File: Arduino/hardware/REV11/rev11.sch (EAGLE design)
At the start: 24 parts, among them IC2 ATMEGA168-AU, Q1 32768Hz

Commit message: updated rev11 as per mark & damons spec's
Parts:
- renumbered FTDI+I2C to I2C_EXT
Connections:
- removed net N$5: I2C_EXT.9, R4.2
- new net N$4: I2C_EXT.11, R4.2
- net GND: now also I2C_EXT.6; no longer I2C_EXT.1, I2C_EXT.3
- net N$1: now also I2C_EXT.5; no longer I2C_EXT.11
- net N$3: now also I2C_EXT.12; no longer I2C_EXT.7
- net RFM_IRQ: now also I2C_EXT.7
- net SCL: now also I2C_EXT.9; no longer I2C_EXT.2
- net SDA: now also I2C_EXT.10; no longer I2C_EXT.4
- net SPI_MISO: now also I2C_EXT.1
- net SPI_MOSI: now also I2C_EXT.4
- net SPI_NSS: now also I2C_EXT.8
- net SPI_SCK: now also I2C_EXT.3
- net VCC: now also I2C_EXT.2; no longer I2C_EXT.14
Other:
- moved on the sheet: C11, R4, R5

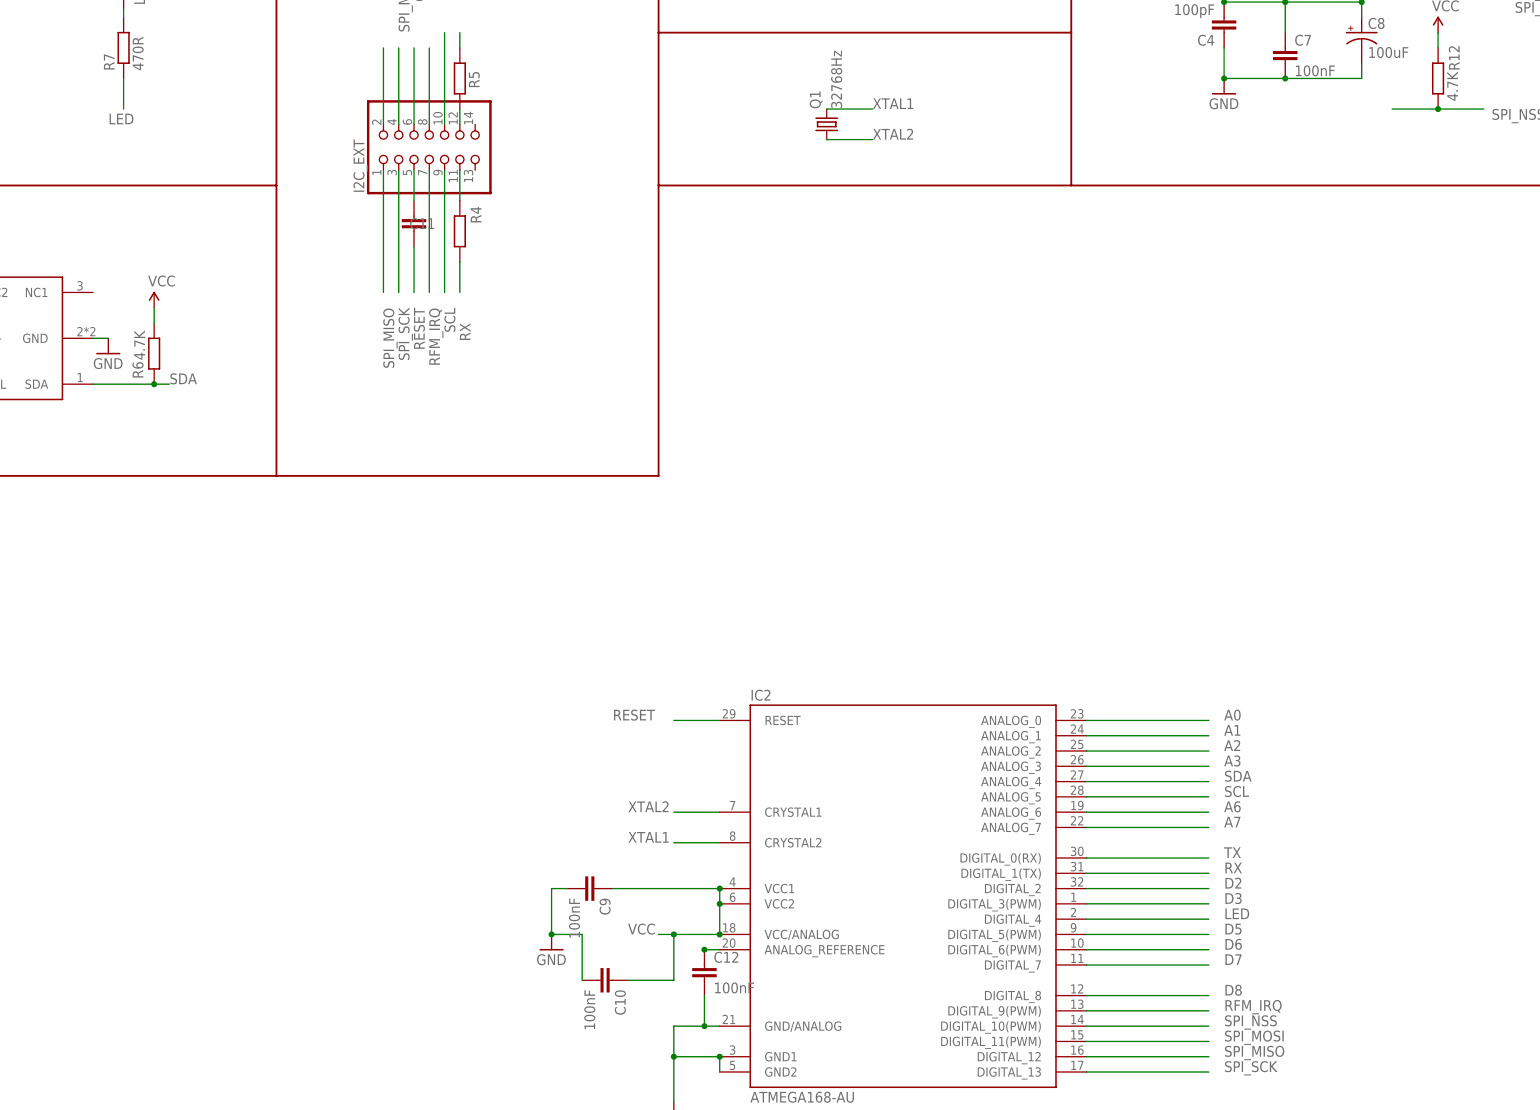
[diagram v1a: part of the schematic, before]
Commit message: updated rev11 as per mark and damon spec 2
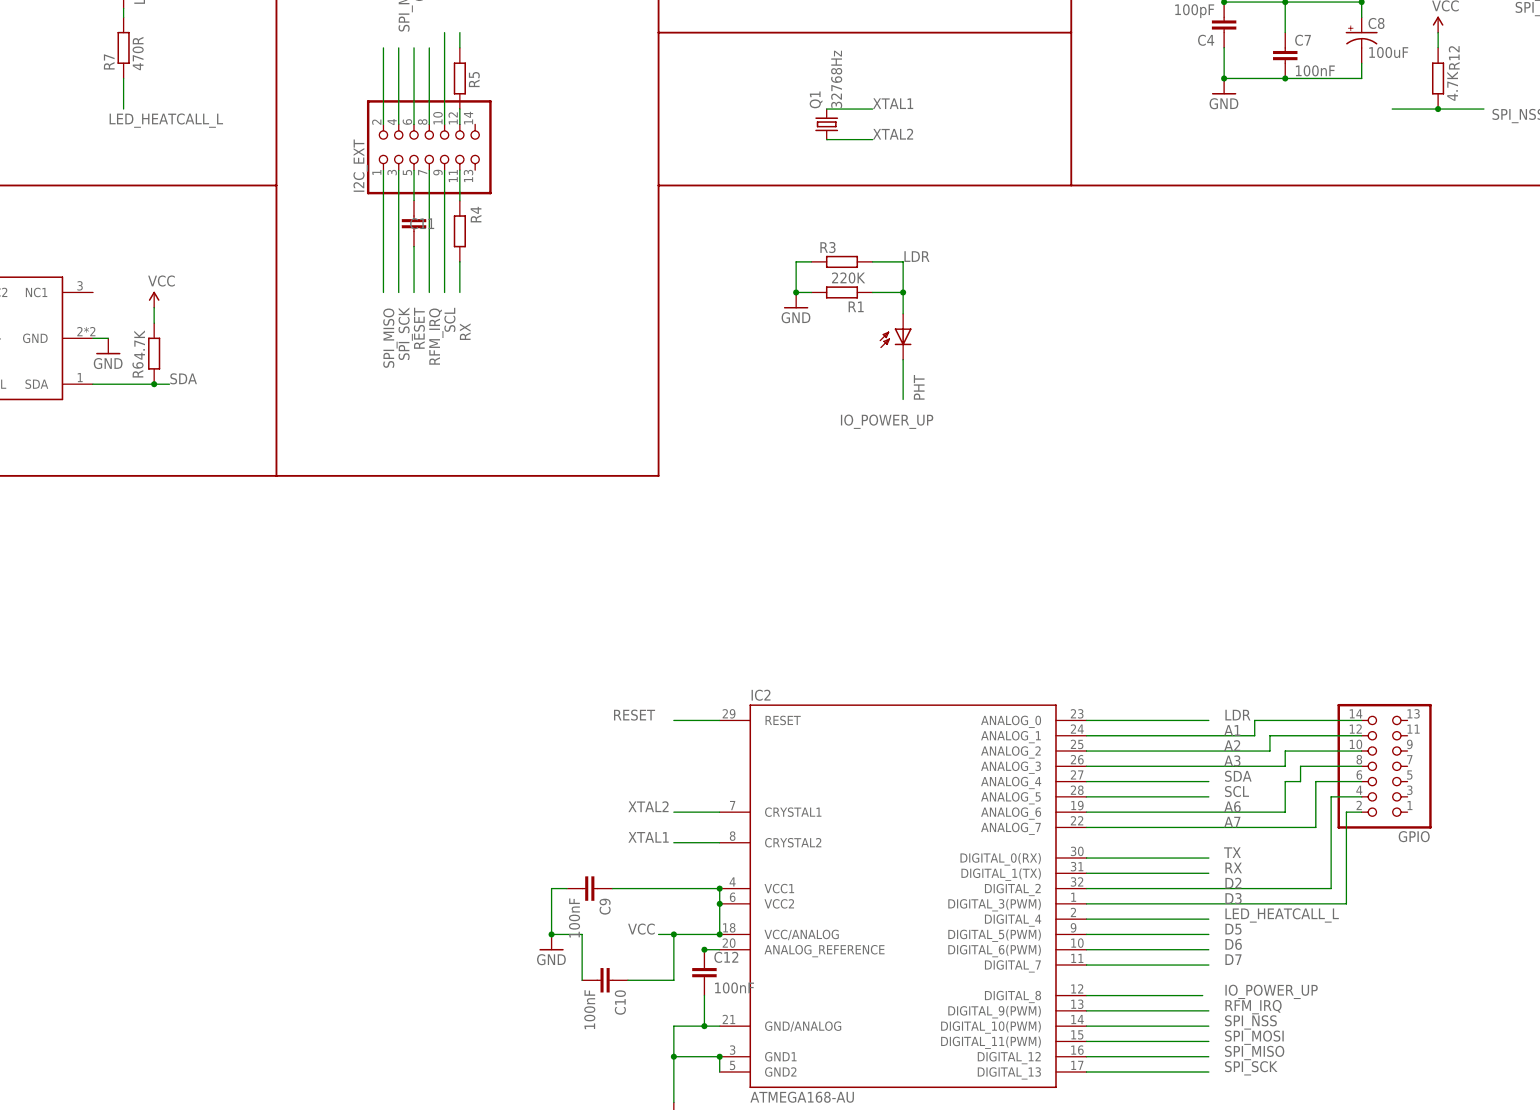
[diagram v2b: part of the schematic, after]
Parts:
- added GPIO: (no value), pinhead:PINHD-2X7
- added PHT: BPX65, opto-trans-siemens:BPX65
- added R1: 220K, resistor:R-EU_R0603
- added R3: (no value), resistor:R-EU_0309/V
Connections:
- net LED renamed LED_HEATCALL_L
- removed net A0: IC2.ANALOG_0
- removed net D8: IC2.DIGITAL_8
- new net IO_POWER_UP: IC2.DIGITAL_8, PHT.C
- new net LDR: IC2.ANALOG_0, PHT.A, R1.1, R3.2
- net GND: now also R1.2, R3.1
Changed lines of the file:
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@@
 <part name="+" library="wirepad" deviceset="2,15/1,0" device=""/>
 <part name="-" library="wirepad" deviceset="2,15/1,0" device=""/>
+<part name="GPIO" library="pinhead" deviceset="PINHD-2X7" device=""/>
+<part name="GND7" library="SparkFun-Aesthetics" deviceset="GND" device=""/>
+<part name="R1" library="resistor" deviceset="R-EU_" device="R0603" value="220K"/>
+<part name="PHT" library="opto-trans-siemens" deviceset="BPX65" device=""/>
+<part name="R3" library="resistor" deviceset="R-EU_" device="0309/V"/>
 </parts>
 <sheets>
@@
 <instance part="+" gate="1" x="12.7" y="238.76"/>
 <instance part="-" gate="1" x="12.7" y="233.68"/>
+<instance part="GPIO" gate="A" x="279.4" y="111.76" rot="R180"/>
+<instance part="GND7" gate="1" x="180.34" y="187.96"/>
+<instance part="R1" gate="G$1" x="187.96" y="190.5" rot="R180"/>
+<instance part="PHT" gate="1" x="198.12" y="184.404" smashed="yes">
+<attribute name="NAME" x="201.676" y="172.466" size="1.778" layer="95" rot="R90"/>
+</instance>
+<instance part="R3" gate="G$1" x="187.96" y="195.58"/>
 </instances>
 <busses>
@@
 <pinref part="I2C_EXT" gate="A" pin="6"/>
 </segment>
+<segment>
+<pinref part="GND7" gate="1" pin="GND"/>
+<wire x1="180.34" y1="190.5" x2="182.88" y2="190.5" width="0.1524" layer="91"/>
+<pinref part="R1" gate="G$1" pin="2"/>
+<pinref part="R3" gate="G$1" pin="1"/>
+<wire x1="182.88" y1="195.58" x2="180.34" y2="195.58" width="0.1524" layer="91"/>
+<wire x1="180.34" y1="195.58" x2="180.34" y2="190.5" width="0.1524" layer="91"/>
+<junction x="180.34" y="190.5"/>
+</segment>
 </net>
 <net name="D6" class="0">
@@
 </segment>
 </net>
-<net name="A0" class="0">
-<segment>
-<wire x1="248.92" y1="119.38" x2="228.6" y2="119.38" width="0.1524" layer="91"/>
-<pinref part="IC2" gate="1" pin="ANALOG_0"/>
-<label x="251.46" y="119.38" size="1.778" layer="95"/>
-</segment>
-</net>
 <net name="A2" class="0">
 <segment>
-<wire x1="248.92" y1="114.3" x2="228.6" y2="114.3" width="0.1524" layer="91"/>
+<wire x1="274.32" y1="116.84" x2="259.08" y2="116.84" width="0.1524" layer="91"/>
+<wire x1="259.08" y1="116.84" x2="259.08" y2="114.3" width="0.1524" layer="91"/>
+<wire x1="259.08" y1="114.3" x2="228.6" y2="114.3" width="0.1524" layer="91"/>
 <pinref part="IC2" gate="1" pin="ANALOG_2"/>
 <label x="251.46" y="114.3" size="1.778" layer="95"/>
@@
 </segment>
 </net>
-<net name="D8" class="0">
-<segment>
-<wire x1="228.6" y1="73.66" x2="248.92" y2="73.66" width="0.1524" layer="91"/>
-<pinref part="IC2" gate="1" pin="DIGITAL_8"/>
-<label x="251.46" y="73.66" size="1.778" layer="95"/>
-</segment>
-</net>
 <net name="D2" class="0">
 <segment>
-<wire x1="248.92" y1="91.44" x2="228.6" y2="91.44" width="0.1524" layer="91"/>
+<wire x1="274.32" y1="106.68" x2="269.24" y2="106.68" width="0.1524" layer="91"/>
+<wire x1="269.24" y1="106.68" x2="269.24" y2="91.44" width="0.1524" layer="91"/>
+<wire x1="269.24" y1="91.44" x2="228.6" y2="91.44" width="0.1524" layer="91"/>
 <pinref part="IC2" gate="1" pin="DIGITAL_2"/>
 <label x="251.46" y="91.44" size="1.778" layer="95"/>
@@
 <segment>
 <pinref part="IC2" gate="1" pin="ANALOG_1"/>
-<wire x1="228.6" y1="116.84" x2="248.92" y2="116.84" width="0.1524" layer="91"/>
+<wire x1="228.6" y1="116.84" x2="256.54" y2="116.84" width="0.1524" layer="91"/>
+<wire x1="256.54" y1="116.84" x2="256.54" y2="119.38" width="0.1524" layer="91"/>
+<wire x1="256.54" y1="119.38" x2="274.32" y2="119.38" width="0.1524" layer="91"/>
 <label x="251.46" y="116.84" size="1.778" layer="95"/>
 </segment>
@@
 <segment>
 <pinref part="IC2" gate="1" pin="DIGITAL_3(PWM)"/>
-<wire x1="228.6" y1="88.9" x2="248.92" y2="88.9" width="0.1524" layer="91"/>
+<wire x1="228.6" y1="88.9" x2="271.78" y2="88.9" width="0.1524" layer="91"/>
+<wire x1="271.78" y1="88.9" x2="271.78" y2="104.14" width="0.1524" layer="91"/>
+<wire x1="271.78" y1="104.14" x2="274.32" y2="104.14" width="0.1524" layer="91"/>
 <label x="251.46" y="88.9" size="1.778" layer="95"/>
 </segment>
@@
 <segment>
 <pinref part="IC2" gate="1" pin="ANALOG_3"/>
-<wire x1="228.6" y1="111.76" x2="248.92" y2="111.76" width="0.1524" layer="91"/>
+<wire x1="228.6" y1="111.76" x2="261.62" y2="111.76" width="0.1524" layer="91"/>
+<wire x1="261.62" y1="111.76" x2="261.62" y2="114.3" width="0.1524" layer="91"/>
+<wire x1="261.62" y1="114.3" x2="274.32" y2="114.3" width="0.1524" layer="91"/>
 <label x="251.46" y="111.76" size="1.778" layer="95"/>
 </segment>
@@
 <segment>
 <pinref part="IC2" gate="1" pin="ANALOG_6"/>
-<wire x1="228.6" y1="104.14" x2="248.92" y2="104.14" width="0.1524" layer="91"/>
+<wire x1="228.6" y1="104.14" x2="261.62" y2="104.14" width="0.1524" layer="91"/>
+<wire x1="261.62" y1="104.14" x2="261.62" y2="109.22" width="0.1524" layer="91"/>
+<wire x1="261.62" y1="109.22" x2="264.16" y2="109.22" width="0.1524" layer="91"/>
+<wire x1="264.16" y1="109.22" x2="264.16" y2="111.76" width="0.1524" layer="91"/>
+<wire x1="264.16" y1="111.76" x2="274.32" y2="111.76" width="0.1524" layer="91"/>
 <label x="251.46" y="104.14" size="1.778" layer="95"/>
 </segment>
@@
 <segment>
 <pinref part="IC2" gate="1" pin="ANALOG_7"/>
-<wire x1="228.6" y1="101.6" x2="248.92" y2="101.6" width="0.1524" layer="91"/>
+<wire x1="228.6" y1="101.6" x2="266.7" y2="101.6" width="0.1524" layer="91"/>
+<wire x1="266.7" y1="101.6" x2="266.7" y2="109.22" width="0.1524" layer="91"/>
+<wire x1="266.7" y1="109.22" x2="274.32" y2="109.22" width="0.1524" layer="91"/>
 <label x="251.46" y="101.6" size="1.778" layer="95"/>
 </segment>
 </net>
-<net name="LED" class="0">
+<net name="LED_HEATCALL_L" class="0">
 <segment>
 <wire x1="228.6" y1="86.36" x2="248.92" y2="86.36" width="0.1524" layer="91"/>
@@
 </segment>
 </net>
+<net name="LDR" class="0">
+<segment>
+<wire x1="198.12" y1="195.58" x2="198.12" y2="190.5" width="0.1524" layer="91"/>
+<pinref part="R1" gate="G$1" pin="1"/>
+<wire x1="198.12" y1="190.5" x2="198.12" y2="186.944" width="0.1524" layer="91"/>
+<wire x1="193.04" y1="190.5" x2="198.12" y2="190.5" width="0.1524" layer="91"/>
+<junction x="198.12" y="190.5"/>
+<pinref part="PHT" gate="1" pin="A"/>
+<pinref part="R3" gate="G$1" pin="2"/>
+<wire x1="198.12" y1="195.58" x2="193.04" y2="195.58" width="0.1524" layer="91"/>
+<label x="198.12" y="195.58" size="1.778" layer="95"/>
+</segment>
+<segment>
+<wire x1="228.6" y1="119.38" x2="248.92" y2="119.38" width="0.1524" layer="91"/>
+<label x="251.46" y="119.38" size="1.778" layer="95"/>
+<pinref part="IC2" gate="1" pin="ANALOG_0"/>
+</segment>
+</net>
+<net name="IO_POWER_UP" class="1">
+<segment>
+<label x="203.2" y="170.18" size="1.778" layer="95" rot="R180"/>
+<pinref part="PHT" gate="1" pin="C"/>
+<wire x1="198.12" y1="179.324" x2="198.12" y2="172.72" width="0.1524" layer="91"/>
+</segment>
+<segment>
+<wire x1="228.6" y1="73.66" x2="247.904" y2="73.66" width="0.1524" layer="91"/>
+<label x="251.46" y="73.66" size="1.778" layer="95"/>
+<pinref part="IC2" gate="1" pin="DIGITAL_8"/>
+</segment>
+</net>

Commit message: added gpio this time
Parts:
- removed GPIO: (no value), pinhead:PINHD-2X7
- added DQ: (no value), wirepad:2,15/1,0
- added JP1: (no value), pinhead:PINHD-1X9
- added R9: 4.7K, resistor:R-EU_R0603
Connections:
- net A1: now also JP1.1
- net A2: now also JP1.2
- net A3: now also JP1.3
- net A6: now also JP1.4
- net A7: now also JP1.5
- net D2: now also DQ.P, R9.1
- net D3: now also JP1.6
- net D5: now also JP1.7
- net D6: now also JP1.8
- net D7: now also JP1.9
- net VCC: now also R9.2

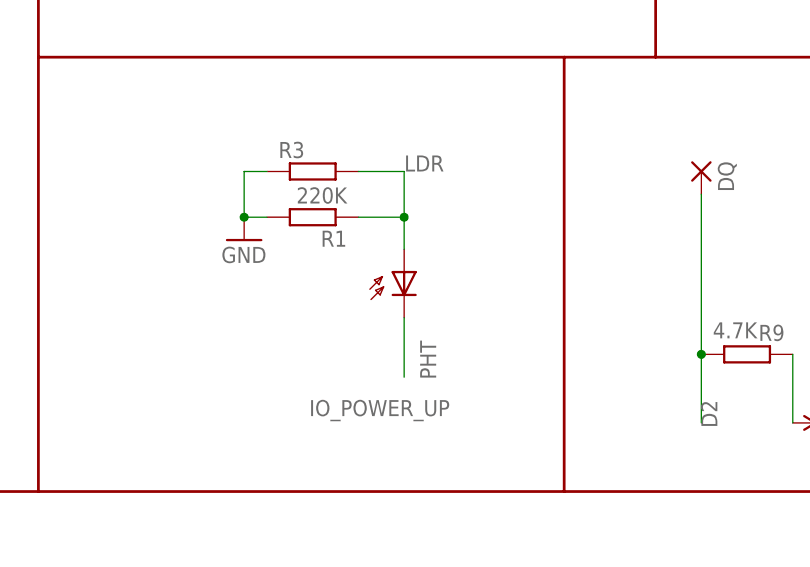
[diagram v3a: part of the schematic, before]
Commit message: rotated LDR
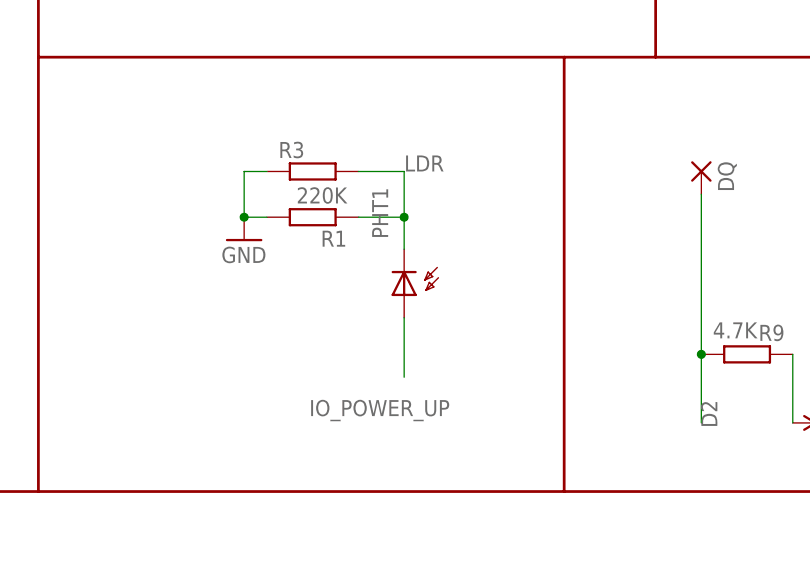
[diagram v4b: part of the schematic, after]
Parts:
- removed PHT: BPX65, opto-trans-siemens:BPX65
- added PHT1: BPX65, opto-trans-siemens:BPX65
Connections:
- net IO_POWER_UP: now also PHT1.A; no longer PHT.C
- net LDR: now also PHT1.C; no longer PHT.A
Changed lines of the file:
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@@
 <part name="GND7" library="SparkFun-Aesthetics" deviceset="GND" device=""/>
 <part name="R1" library="resistor" deviceset="R-EU_" device="R0603" value="220K"/>
-<part name="PHT" library="opto-trans-siemens" deviceset="BPX65" device=""/>
 <part name="R3" library="resistor" deviceset="R-EU_" device="0309/V"/>
 <part name="R9" library="resistor" deviceset="R-EU_" device="R0603" value="4.7K"/>
@@
 <part name="DQ" library="wirepad" deviceset="2,15/1,0" device=""/>
 <part name="JP1" library="pinhead" deviceset="PINHD-1X9" device=""/>
+<part name="PHT1" library="opto-trans-siemens" deviceset="BPX65" device=""/>
 </parts>
 <sheets>
@@
 <instance part="GND7" gate="1" x="180.34" y="187.96"/>
 <instance part="R1" gate="G$1" x="187.96" y="190.5" rot="R180"/>
-<instance part="PHT" gate="1" x="198.12" y="184.404" smashed="yes">
-<attribute name="NAME" x="201.676" y="172.466" size="1.778" layer="95" rot="R90"/>
-</instance>
 <instance part="R3" gate="G$1" x="187.96" y="195.58"/>
 <instance part="R9" gate="G$1" x="236.22" y="175.26" smashed="yes">
@@
 <instance part="DQ" gate="1" x="231.14" y="195.58" rot="R270"/>
 <instance part="JP1" gate="A" x="297.18" y="109.22"/>
+<instance part="PHT1" gate="1" x="198.12" y="181.864" smashed="yes" rot="R180">
+<attribute name="NAME" x="194.564" y="193.802" size="1.778" layer="95" rot="R270"/>
+</instance>
 </instances>
 <busses>
@@
 <wire x1="193.04" y1="190.5" x2="198.12" y2="190.5" width="0.1524" layer="91"/>
 <junction x="198.12" y="190.5"/>
-<pinref part="PHT" gate="1" pin="A"/>
 <pinref part="R3" gate="G$1" pin="2"/>
 <wire x1="198.12" y1="195.58" x2="193.04" y2="195.58" width="0.1524" layer="91"/>
 <label x="198.12" y="195.58" size="1.778" layer="95"/>
+<pinref part="PHT1" gate="1" pin="C"/>
 </segment>
 <segment>
@@
 <segment>
 <label x="203.2" y="170.18" size="1.778" layer="95" rot="R180"/>
-<pinref part="PHT" gate="1" pin="C"/>
 <wire x1="198.12" y1="179.324" x2="198.12" y2="172.72" width="0.1524" layer="91"/>
-</segment>
-<segment>
+<pinref part="PHT1" gate="1" pin="A"/>
+</segment>
+<segment>
